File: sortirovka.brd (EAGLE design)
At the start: 86.7 x 86.7 mm, 72 parts, among them IC1 DS1307Z, IC3 LM1117IMPX-3.3, U1 MAX3485CSA, X1 PI3-CON, X10 MKDSN1,5/3-5,08, X3 MKDSN1,5/4-5,08, X4 MKDSN1,5/2-5,08, X5 22-23-2021, X6 22-23-2051, X7 22-23-2041, X8 22-23-2051, X9 MKDSN1,5/7-5,08

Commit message: initial
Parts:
- removed C2, C4: (no value), rcl:E3,5-8
- removed C3: 0.1, rcl:C0805
- removed D10, D5, D6, D7, D8, D9: DIODE1N4007, MyLib:SMA-DIODE
- removed IC1: DS1307Z, MyLib:SOIC8
- removed IC3: LM1117IMPX-3.3, lm1117:SOT223
- removed OC1, OC2, OC3, OC4, OC5, OC6: (no value), MyLib:SFH6106
- removed Q1: (no value), MyLib:SOT23-6
- removed Q5: (no value), MyLib:MA306
- removed R10, R11: 3k3, rcl:R0805
- removed R12, R13: 1k, rcl:R0805
- removed R14: 0, rcl:R0805
- removed R16, R17: 15, rcl:0207/10
- removed R18, R19: 1k5, rcl:0207/10
- removed R20: 10, rcl:0207/10
- removed U$1, U$2, U$4, U$5, U$6, U$7: NSI45020AT1GSOD-123, MyLib:SOD123
- removed X5: 22-23-2021, con-molex:22-23-2021
- removed X7: 22-23-2041, con-molex:22-23-2041
- removed X8: 22-23-2051, con-molex:22-23-2051
- removed X9: MKDSN1,5/7-5,08, con-phoenix-508:MKDSN1,5/7-5,08
- added JP1: (no value), pinhead:1X04
- added PWS1: TEN_32410, traco-electronic:TEN3XXXX
- added Q2: (no value), MyLib:SOT23-6
- C1: value (none) -> 0.1; device rcl:E3,5-8 -> rcl:C0805
- R5, R6: value 1k -> 1k5
- R7: value 0 -> 15
- R8: value 1k -> 15
- R9: value 1k -> 10
- X1: value PI3-CON -> PI3-CONMINIBOARD; device MyLib:RPI3 -> MyLib:RPI3_MINIBOARD
- moved C7 110.4 mm to (-49.1, 63.9), turned to 90 degrees
- moved C5 70.0 mm to (-49.0, 58.5)
- moved C9 62.9 mm to (-53.5, 58.3), turned to 270 degrees
- moved C6 62.4 mm to (-5.27, 25.8)
- moved D1 58.0 mm to (12.6, 21.7)
- moved D2 58.0 mm to (5.21, 21.7)
- moved D3 58.0 mm to (-2.16, 22.0)
- moved D4 58.0 mm to (19.7, 21.7)
- moved OC10 58.0 mm to (21.0, 31.6)
- moved OC7 58.0 mm to (-0.89, 31.6)
- moved OC8 58.0 mm to (6.48, 31.6)
- moved OC9 58.0 mm to (13.9, 31.6)
- moved X3 55.3 mm to (11.6, 15.0)
- moved C1 53.5 mm to (32.6, 18.6), flipped to the bottom, turned to 180 degrees
- moved X1 51.6 mm to (-6.60, 75.4)
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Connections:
- net N$1 renamed TX
- net N$2 renamed RX
- net N$3 renamed R/E
- removed net N$16: D5.C, OC1.1, U$1.C
- removed net N$17: D6.C, OC2.1, U$2.C
- removed net N$20: G1.+, IC1.3
- removed net N$21: U$1.A, X9.7
- removed net N$22: U$2.A, X9.6
- removed net N$23: IC1.1, Q5.1
- removed net N$24: D7.C, OC3.1, U$4.C
- removed net N$25: IC1.2, Q5.4
- removed net N$26: IC1.6, R10.1, X1.P$5, X7.3
- removed net N$27: IC1.5, R11.1, X1.P$3, X7.2
- removed net N$30: D8.C, OC4.1, U$5.C
- removed net N$32: D9.C, OC5.1, U$6.C
- removed net N$33: U$5.A, X9.4
- removed net N$34: OC6.4, R13.2, X1.P$37
- removed net N$35: U$4.A, X9.5
- removed net N$36: D10.C, OC6.1, U$7.C
- removed net N$37: U$6.A, X9.3
- removed net N$38: U$7.A, X9.2
- removed net N$39: OC5.4, R12.2, X1.P$35
- removed net N$40: OC4.4, R9.2, X1.P$33
- removed net N$41: OC3.4, R8.2, X1.P$31
- removed net N$42: OC2.4, R6.2, X1.P$29
- removed net N$43: OC1.4, R5.2, X1.P$7
- removed net N$48: Q1.1, Q1.2, Q1.5, Q1.6, X5.1
- removed net N$8: R3.2, X1.P$36
- removed net N$9: R4.2, X1.P$32
- removed net PW: C2.+, C3.1, IC3.3, Q1.4, R14.2
- new net N$1: R3.2, X1.P$38
- new net N$2: R4.2, X1.P$40
- new net SCL: JP1.3, X1.P$5
- new net SDA: JP1.4, X1.P$3
- net +24V: now also C1.1, PWS1.22, PWS1.23, X4.2; no longer C4.+, X4.1
- net +3V3: now also PWS1.14, R6.1, X1.P$1, X1.P$17; no longer C1.+, IC1.8, IC3.2, IC3.TAB, OC1.3, OC2.3, OC3.3, OC4.3, OC5.3, OC6.3, R10.2, R11.2, R19.2, R7.2, X7.1
- net GND: now also JP1.1, PWS1.16, R5.2; no longer C1.-, C2.-, C3.2, G1.-, IC1.4, IC3.1, Q1.3, R12.1, R13.1, R18.1, R20.2, R5.1, R6.1, R8.1, X5.2, X7.4, X8.5
- net GND1: now also C1.2, PWS1.2, PWS1.3, Q2.3, X4.1; no longer C4.-, D10.A, D5.A, D6.A, D7.A, D8.A, D9.A, OC1.2, OC2.2, OC3.2, OC4.2, OC5.2, OC6.2, X4.2, X9.1
- net MISO: no longer X8.2
- net MOSI: no longer X8.3
- net N$14: now also Q2.1, Q2.2, Q2.5, Q2.6; no longer R7.1, X1.P$1, X1.P$17
- net N$28: no longer R14.1
- net N$4: now also R5.1, R7.1; no longer R16.2, R18.2
- net N$45: now also R7.2, X10.1; no longer R16.1, X10.2
- net N$46: now also R8.2, X10.2; no longer R17.1, X10.1
- net N$47: now also R6.2, R8.1; no longer R17.2, R19.1
- net N$5: now also R9.2; no longer R20.1
- net N$6: now also X1.P$32; no longer X1.P$40
- net N$7: now also X1.P$36; no longer X1.P$38
- net SPI1: no longer X8.4
- net SPI_CLK: no longer X8.1
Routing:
- net +3V3: track 262.8 -> 50.3 mm, vias 2 -> 4
- net GND1: track 225.8 -> 115.1 mm, vias 0 -> 2
- net GND: track 217.7 -> 298.9 mm, vias 12 -> 0
- net N$26: track 69.0 -> 0.00 mm
- net N$27: track 65.8 -> 0.00 mm
- net SPI0: track 0.00 -> 63.7 mm
- net PW: track 61.3 -> 0.00 mm
- net N$43: track 57.5 -> 0.00 mm, vias 2 -> 0
- net SDA: track 0.00 -> 49.5 mm, vias 0 -> 2
- net SCL: track 0.00 -> 47.8 mm, vias 0 -> 2
- net N$15: track 4.39 -> 51.2 mm
- net N$42: track 42.2 -> 0.00 mm
- net N$41: track 36.3 -> 0.00 mm
- net N$9: track 33.5 -> 0.00 mm
- net N$18: track 2.60 -> 35.6 mm
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- removed copper zone on layer 16, net GND
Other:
- board outline removed

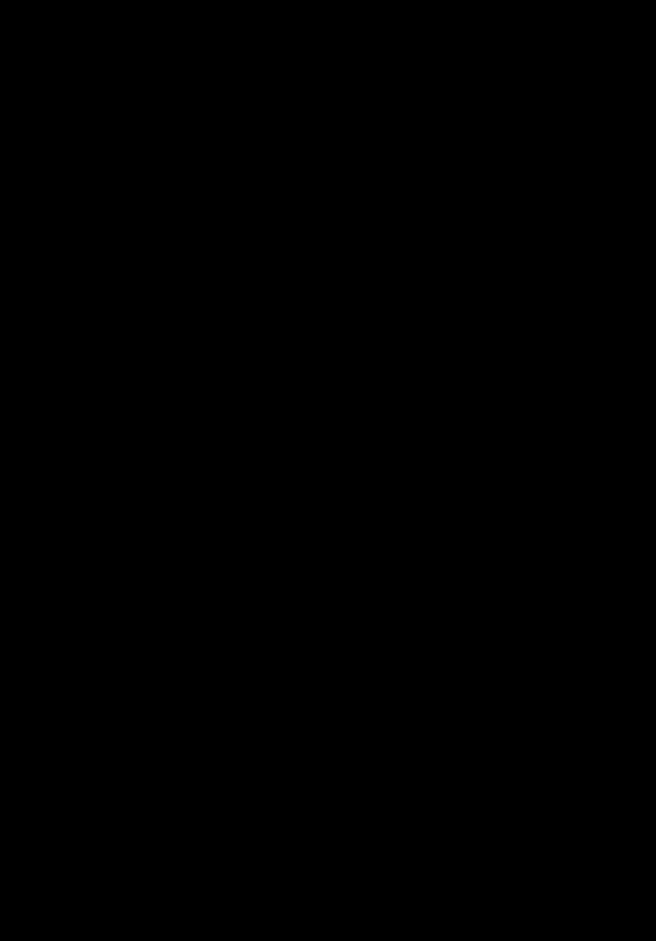
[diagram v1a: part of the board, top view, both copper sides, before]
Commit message: Add I2C RTC
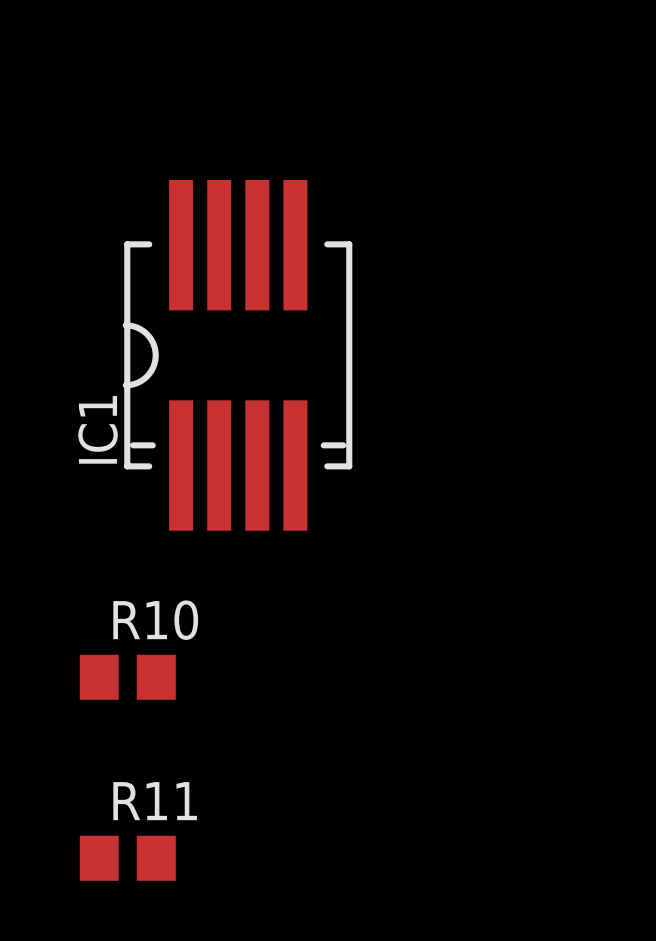
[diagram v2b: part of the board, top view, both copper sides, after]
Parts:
- added IC1: DS1307/PCF8583, MyLib:SO8-7_5+SOIC8
- added R10, R11: 3k3, rcl:R0805
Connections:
- new net N$3: G1.+, IC1.3
- net +3V3: now also IC1.8, R10.2, R11.2
- net GND: now also G1.-, IC1.4
- net SCL: now also IC1.6, R10.1
- net SDA: now also IC1.5, R11.1
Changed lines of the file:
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@@
 <element name="JP1" library="pinhead" package="1X04" value="" x="-3.1115" y="60.6425" rot="R90"/>
 <element name="C1" library="rcl" package="C0805" value="0.1" x="32.639" y="18.6055" rot="MR180"/>
+<element name="IC1" library="MyLib" package="SO8-7_5+SOIC8" value="DS1307/PCF8583" x="-73.279" y="11.7475"/>
+<element name="R10" library="rcl" package="R0805" value="3k3" x="-76.962" y="1.016"/>
+<element name="R11" library="rcl" package="R0805" value="3k3" x="-76.962" y="-5.0165"/>
 </elements>
 <signals>
@@
 <wire x1="25.7175" y1="55.3745" x2="27.7495" y2="55.3745" width="0.4064" layer="16"/>
 <wire x1="25.7175" y1="50.927" x2="25.7175" y2="55.3745" width="0.4064" layer="16"/>
-<wire x1="-49.149" y1="62.9945" x2="24.8285" y2="55.3745" width="0" layer="19" extent="1-16"/>
-<wire x1="24.8285" y1="55.3745" x2="25.7175" y2="55.3745" width="0" layer="19" extent="1-16"/>
 <wire x1="44.6278" y1="46.7614" x2="43.7642" y2="47.625" width="0.4064" layer="16"/>
 <wire x1="43.7642" y1="47.625" x2="42.037" y2="47.625" width="0.4064" layer="16"/>
@@
 <wire x1="29.0195" y1="49.718" x2="29.0195" y2="50.927" width="0.4064" layer="16"/>
 <wire x1="29.0195" y1="50.927" x2="25.7175" y2="50.927" width="0.4064" layer="16"/>
+<contactref element="IC1" pad="8"/>
+<contactref element="R11" pad="2"/>
+<contactref element="R10" pad="2"/>
 <wire x1="27.7495" y1="55.3745" x2="31.49" y2="55.6895" width="0" layer="19" extent="16-16"/>
-<wire x1="-48.9585" y1="59.4335" x2="-49.149" y2="62.9945" width="0" layer="19" extent="16-16"/>
-<wire x1="-44.1325" y1="58.989" x2="-48.9585" y2="59.4335" width="0" layer="19" extent="16-16"/>
+<wire x1="-44.1325" y1="58.989" x2="25.7175" y2="55.3745" width="0" layer="19" extent="16-16"/>
+<wire x1="-48.9585" y1="59.4335" x2="-44.1325" y2="58.989" width="0" layer="19" extent="16-16"/>
+<wire x1="-49.149" y1="62.9945" x2="-48.9585" y2="59.4335" width="0" layer="19" extent="16-16"/>
 <wire x1="-53.467" y1="59.243" x2="-48.9585" y2="59.4335" width="0" layer="19" extent="16-16"/>
+<wire x1="-75.184" y1="15.42" x2="-53.467" y2="59.243" width="0" layer="19" extent="1-16"/>
+<wire x1="-76.012" y1="1.016" x2="-75.184" y2="15.42" width="0" layer="19" extent="1-1"/>
+<wire x1="-76.012" y1="-5.0165" x2="-76.012" y2="1.016" width="0" layer="19" extent="1-1"/>
 </signal>
 <signal name="GND">
@@
 <wire x1="35.1765" y1="65.9765" x2="35.179" y2="65.974" width="0.4064" layer="16"/>
 <wire x1="25.7175" y1="45.847" x2="23.1775" y2="45.847" width="0.4064" layer="16"/>
-<wire x1="23.1775" y1="62.291" x2="23.1775" y2="67.7545" width="0" layer="19" extent="1-16"/>
 <wire x1="23.1775" y1="67.7545" x2="23.1775" y2="45.847" width="0.4064" layer="16"/>
 <wire x1="23.1775" y1="75.2475" x2="23.1775" y2="67.7545" width="0.4064" layer="16"/>
@@
 <wire x1="25.847" y1="67.6275" x2="25.847" y2="67.7545" width="0.4064" layer="16"/>
 <wire x1="25.847" y1="67.7545" x2="23.1775" y2="67.7545" width="0.4064" layer="16"/>
-<wire x1="-49.149" y1="64.8945" x2="23.1775" y2="62.291" width="0" layer="19" extent="1-16"/>
 <wire x1="47.1678" y1="51.8414" x2="45.9359" y2="50.6095" width="0.4064" layer="16"/>
 <wire x1="45.9359" y1="50.6095" x2="43.3705" y2="50.6095" width="0.4064" layer="16"/>
@@
 <wire x1="44.6278" y1="56.9214" x2="45.9359" y2="58.2295" width="0.4064" layer="16"/>
 <wire x1="45.9359" y1="58.2295" x2="49.2125" y2="58.2295" width="0.4064" layer="16"/>
-<wire x1="-53.467" y1="57.343" x2="-6.4135" y2="33.782" width="0" layer="19" extent="16-16"/>
-<wire x1="-48.9585" y1="57.5335" x2="-53.467" y2="57.343" width="0" layer="19" extent="16-16"/>
-<wire x1="-44.1325" y1="57.089" x2="-48.9585" y2="57.5335" width="0" layer="19" extent="16-16"/>
+<contactref element="IC1" pad="4"/>
+<contactref element="G1" pad="-"/>
+<wire x1="23.1775" y1="67.7545" x2="12.827" y2="70.2945" width="0" layer="19" extent="16-16"/>
+<wire x1="-44.1325" y1="57.089" x2="-6.4135" y2="56.769" width="0" layer="19" extent="16-16"/>
+<wire x1="-48.9585" y1="57.5335" x2="-44.1325" y2="57.089" width="0" layer="19" extent="16-16"/>
+<wire x1="-53.467" y1="57.343" x2="-48.9585" y2="57.5335" width="0" layer="19" extent="16-16"/>
+<wire x1="-49.149" y1="64.8945" x2="-48.9585" y2="57.5335" width="0" layer="19" extent="16-16"/>
+<wire x1="-71.374" y1="8.075" x2="-53.467" y2="57.343" width="0" layer="19" extent="1-16"/>
 </signal>
 <signal name="N$6">
@@
 <via x="0.1905" y="64.4525" extent="1-16" drill="0.6" shape="square"/>
 <wire x1="0.1905" y1="64.4525" x2="-3.1115" y2="64.4525" width="0.4064" layer="16"/>
+<contactref element="IC1" pad="5"/>
+<contactref element="R11" pad="1"/>
+<wire x1="-71.374" y1="15.42" x2="-77.912" y2="-5.0165" width="0" layer="19" extent="1-1"/>
+<wire x1="-3.1115" y1="64.4525" x2="-71.374" y2="15.42" width="0" layer="19" extent="1-1"/>
 </signal>
 <signal name="SCL">
@@
 <wire x1="0.254" y1="61.976" x2="-3.1115" y2="61.976" width="0.4064" layer="16"/>
 <wire x1="-3.1115" y1="61.976" x2="-3.1115" y2="61.9125" width="0.4064" layer="16"/>
+<contactref element="IC1" pad="6"/>
+<contactref element="R10" pad="1"/>
+<wire x1="-72.644" y1="15.42" x2="-77.912" y2="1.016" width="0" layer="19" extent="1-1"/>
+<wire x1="-3.1115" y1="61.9125" x2="-72.644" y2="15.42" width="0" layer="19" extent="1-1"/>
+</signal>
+<signal name="N$3">
+<contactref element="IC1" pad="3"/>
+<contactref element="G1" pad="+"/>
+<wire x1="12.827" y1="50.927" x2="-72.644" y2="8.075" width="0" layer="19" extent="1-1"/>
 </signal>
 </signals>

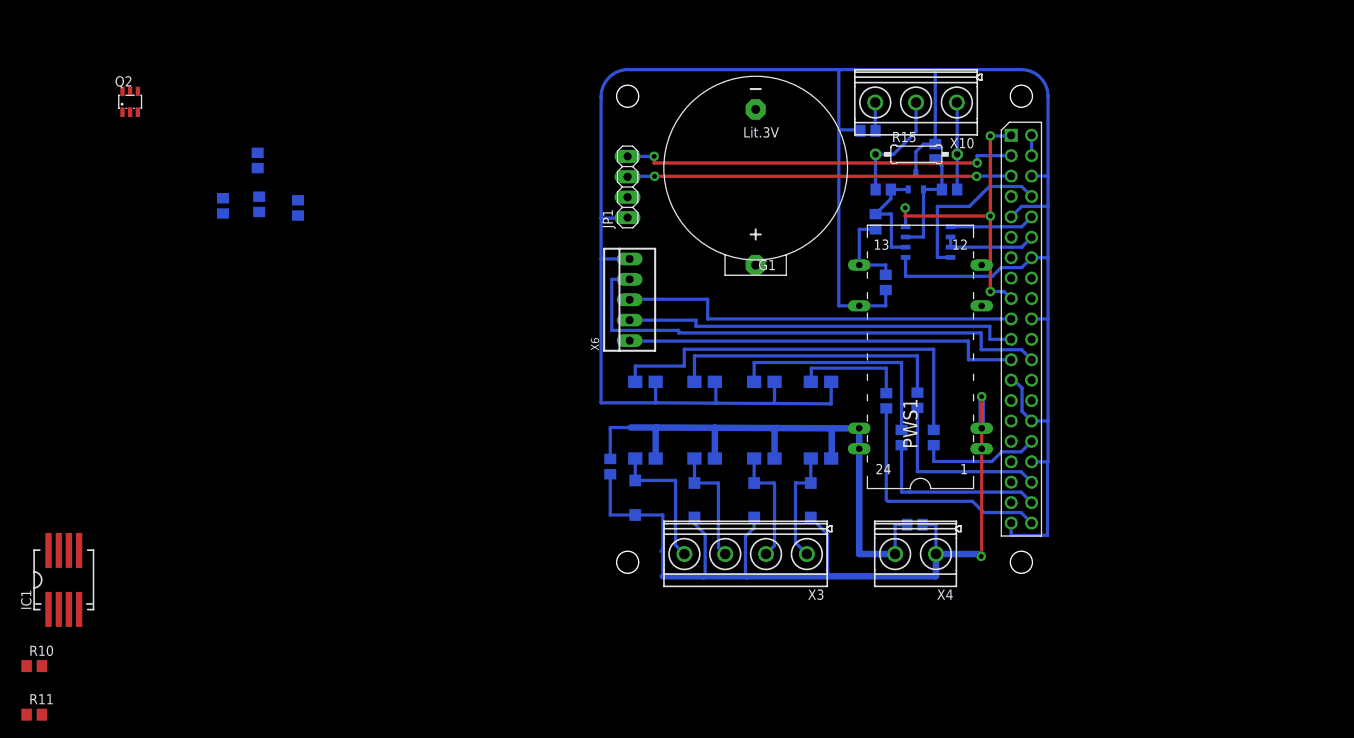
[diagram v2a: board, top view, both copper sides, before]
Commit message: traced I2C
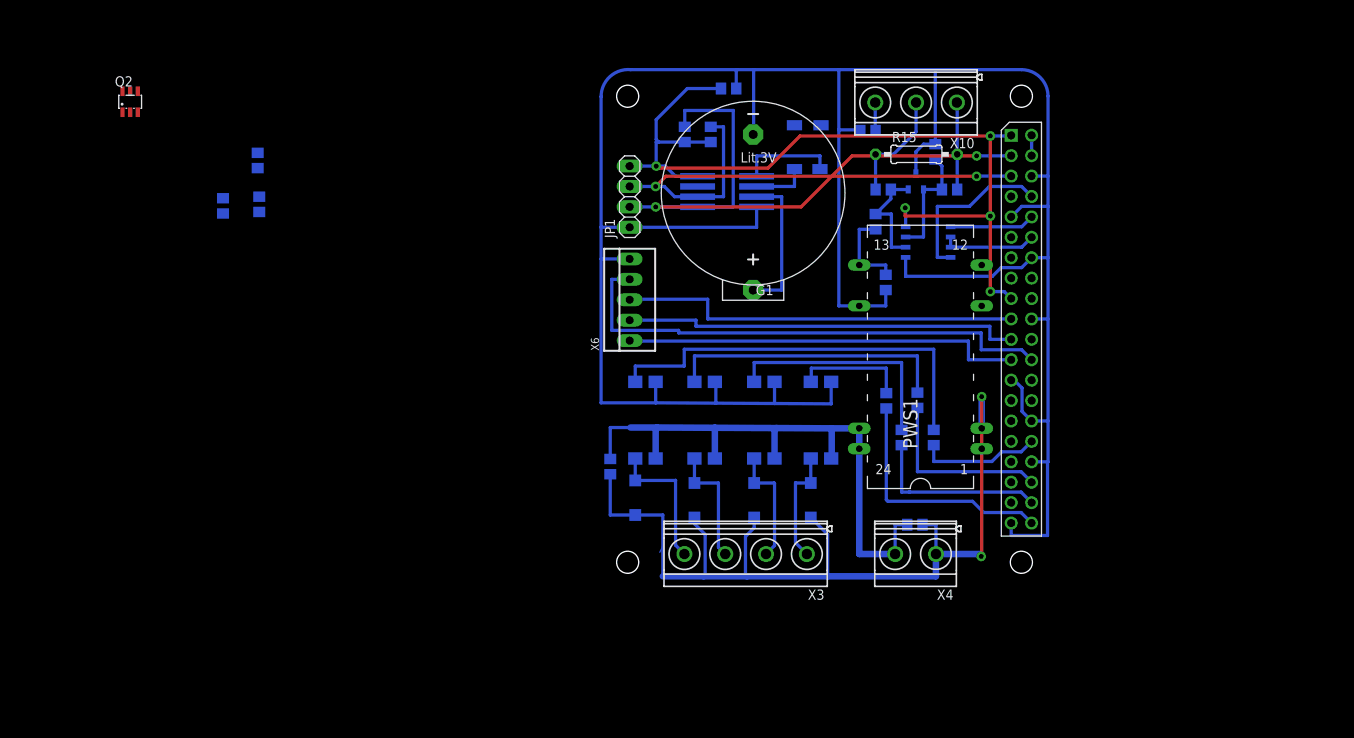
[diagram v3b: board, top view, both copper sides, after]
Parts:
- added Q1: (no value), MyLib:MA306
- moved R11 108.5 mm to (4.00, 67.2), flipped to the bottom, turned to 270 degrees
- moved R10 107.1 mm to (7.24, 67.2), flipped to the bottom, turned to 270 degrees
- moved IC1 95.7 mm to (9.27, 60.1), flipped to the bottom, turned to 270 degrees
- moved C8 55.6 mm to (9.46, 72.9), turned to 180 degrees
- moved G1 3.13 mm to (12.5, 59.9)
- moved JP1 1.23 mm to (-2.86, 59.4)
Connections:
- new net N$8: IC1.1, Q1.4
- new net N$9: IC1.2, Q1.1
- net +3V3: now also JP1.4
- net SDA: now also JP1.2; no longer JP1.4
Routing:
- net +3V3: track 50.3 -> 125.0 mm, vias 4 -> 5
- net SDA: track 49.5 -> 79.9 mm
- net GND: track 298.9 -> 328.2 mm
- net SCL: track 47.8 -> 67.3 mm
- net N$3: track 0.00 -> 18.3 mm
- net N$8: track 0.00 -> 12.1 mm
- net N$9: track 0.00 -> 6.87 mm

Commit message: wip
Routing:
- net GND: track 328.2 -> 317.7 mm
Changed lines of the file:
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@@
 <wire x1="25.847" y1="67.6275" x2="25.847" y2="67.7545" width="0.4064" layer="16"/>
 <wire x1="25.847" y1="67.7545" x2="23.1775" y2="67.7545" width="0.4064" layer="16"/>
-<wire x1="47.1678" y1="51.8414" x2="45.9359" y2="50.6095" width="0.4064" layer="16"/>
-<wire x1="45.9359" y1="50.6095" x2="43.3705" y2="50.6095" width="0.4064" layer="16"/>
-<wire x1="43.3705" y1="50.6095" x2="42.291" y2="49.53" width="0.4064" layer="16"/>
-<wire x1="42.291" y1="49.53" x2="31.496" y2="49.53" width="0.4064" layer="16"/>
-<wire x1="31.496" y1="49.53" x2="31.49" y2="49.536" width="0.4064" layer="16"/>
-<wire x1="31.49" y1="49.536" x2="31.49" y2="51.8795" width="0.4064" layer="16"/>
 <wire x1="49.149" y1="26.4414" x2="47.1678" y2="26.4414" width="0.4064" layer="16"/>
 <wire x1="49.2125" y1="26.4414" x2="49.2125" y2="31.5214" width="0.4064" layer="16"/>
@@
 <wire x1="44.9961" y1="36.6014" x2="44.6278" y2="36.6014" width="0.4064" layer="16"/>
 <contactref element="JP1" pad="1"/>
-<wire x1="29.0195" y1="47.818" x2="29.0195" y2="45.847" width="0.4064" layer="16"/>
+<wire x1="29.0195" y1="45.847" x2="29.0195" y2="47.818" width="0.4064" layer="16"/>
 <wire x1="29.0195" y1="45.847" x2="25.7175" y2="45.847" width="0.4064" layer="16"/>
 <wire x1="44.6278" y1="56.9214" x2="45.9359" y2="58.2295" width="0.4064" layer="16"/>
@@
 <wire x1="10.4115" y1="72.898" x2="10.4115" y2="75.118" width="0.4064" layer="16"/>
 <wire x1="10.4115" y1="75.118" x2="10.541" y2="75.2475" width="0.4064" layer="16"/>
+<wire x1="31.49" y1="51.8795" x2="31.49" y2="45.847" width="0.4064" layer="16"/>
+<wire x1="31.49" y1="45.847" x2="29.0195" y2="45.847" width="0.4064" layer="16"/>
 <wire x1="-48.9585" y1="57.5335" x2="-6.4135" y2="55.626" width="0" layer="19" extent="16-16"/>
 <wire x1="-53.467" y1="57.343" x2="-48.9585" y2="57.5335" width="0" layer="19" extent="16-16"/>
@@
 <wire x1="40.894" y1="40.386" x2="40.894" y2="42.4815" width="0.4064" layer="16"/>
 <wire x1="3.2385" y1="42.4815" x2="40.894" y2="42.4815" width="0.4064" layer="16"/>
-<wire x1="3.2385" y1="42.4815" x2="0.508" y2="42.4815" width="0" layer="19" extent="1-16"/>
 <wire x1="-2.8575" y1="49.149" x2="-5.08" y2="49.149" width="0.4064" layer="16"/>
 <wire x1="-5.08" y1="49.149" x2="-5.08" y2="42.799" width="0.4064" layer="16"/>
@@
 <wire x1="-2.159" y1="36.393" x2="-2.1565" y2="36.3955" width="0.4064" layer="16"/>
 <wire x1="-2.1565" y1="36.393" x2="-2.159" y2="36.393" width="0.4064" layer="16"/>
-<wire x1="34.925" y1="40.4495" x2="37.719" y2="40.4495" width="0" layer="19" extent="1-16"/>
 <wire x1="34.9885" y1="40.4495" x2="3.937" y2="40.4495" width="0.4064" layer="16"/>
 <wire x1="3.937" y1="40.4495" x2="3.937" y2="38.354" width="0.4064" layer="16"/>
@@
 <wire x1="-2.159" y1="38.354" x2="-2.159" y2="36.393" width="0.4064" layer="16"/>
 <wire x1="34.9885" y1="30.414" x2="34.9885" y2="40.4495" width="0.4064" layer="16"/>
-<wire x1="34.9885" y1="40.4495" x2="34.925" y2="40.4495" width="0" layer="19" extent="1-16"/>
 </signal>
 <signal name="N$18">
@@
 <wire x1="5.2045" y1="36.393" x2="5.207" y2="36.393" width="0.4064" layer="16"/>
 <wire x1="5.2095" y1="36.3955" x2="5.207" y2="36.393" width="0.4064" layer="16"/>
-<wire x1="32.893" y1="39.624" x2="34.8615" y2="39.624" width="0" layer="19" extent="1-16"/>
 <wire x1="32.9565" y1="39.624" x2="5.207" y2="39.624" width="0.4064" layer="16"/>
 <wire x1="5.207" y1="39.624" x2="5.207" y2="36.393" width="0.4064" layer="16"/>
 <wire x1="32.9565" y1="35.0495" x2="32.9565" y2="39.624" width="0.4064" layer="16"/>
-<wire x1="32.9565" y1="39.624" x2="32.893" y2="39.624" width="0" layer="19" extent="1-16"/>
 </signal>
 <signal name="N$19">
@@
 <wire x1="12.639" y1="36.3955" x2="12.6365" y2="36.393" width="0.4064" layer="16"/>
 <wire x1="12.5755" y1="36.393" x2="12.6365" y2="36.393" width="0.4064" layer="16"/>
-<wire x1="30.988" y1="38.7985" x2="32.004" y2="38.7985" width="0" layer="19" extent="1-16"/>
 <wire x1="30.988" y1="38.7985" x2="12.6365" y2="38.7985" width="0.4064" layer="16"/>
 <wire x1="12.6365" y1="38.7985" x2="12.6365" y2="36.393" width="0.4064" layer="16"/>
